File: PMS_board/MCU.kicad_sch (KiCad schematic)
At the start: 0 parts

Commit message: added buzzer? looked into stuff
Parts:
- added U13: STM32H563RITx, Package_QFP:LQFP-64_10x10mm_P0.5mm, symbol MCU_ST_STM32H5:STM32H563RITx
- added U6: (no value), MRDT_Shields:RoveNode_H5, symbol MRDT_Shields:RoveNode_H5
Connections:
- new net: U13.18 (VSS), U13.31 (VSS), U13.47 (VSS), U13.63 (VSS)
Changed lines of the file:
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@@
 	(generator_version "10.0")
 	(paper "A4")
-)

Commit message: TryingToFigureOutRoveNode
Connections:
- net PMSBus: now reaches U6.1 (VIN)
- net GND: now reaches U6.2 (GND)
- net out to Display: now reaches U6.23 (LED2)
- net out to Display: now also U6.24 (LED1), U6.42 (PB0), U6.43 (PB1)
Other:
- note added: "what is going on for microcontroller?"
- moved on the sheet: U13

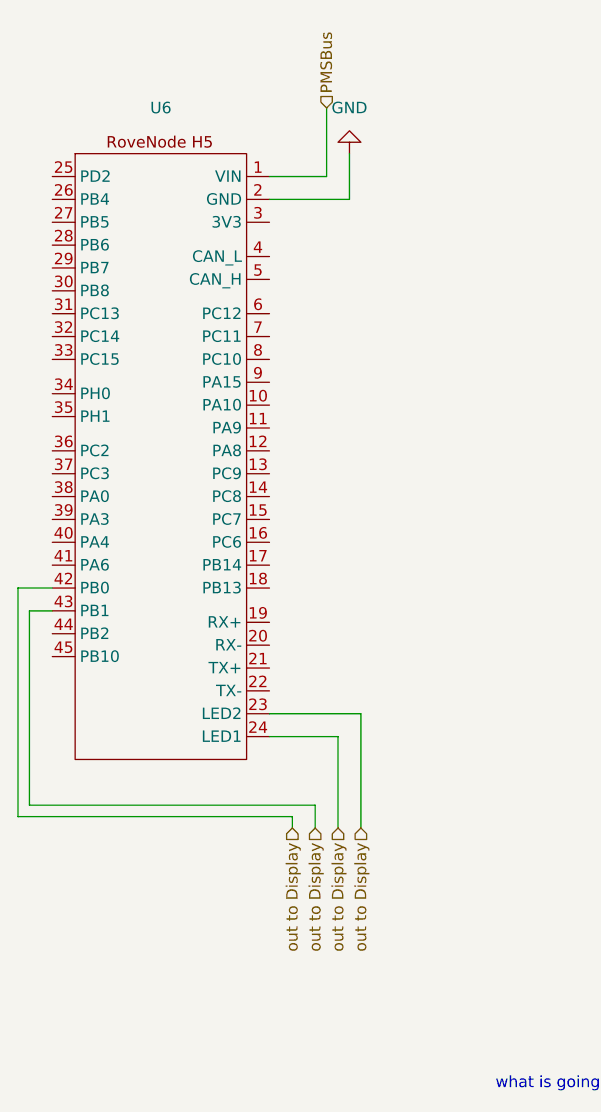
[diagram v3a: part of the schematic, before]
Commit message: addeddisplay
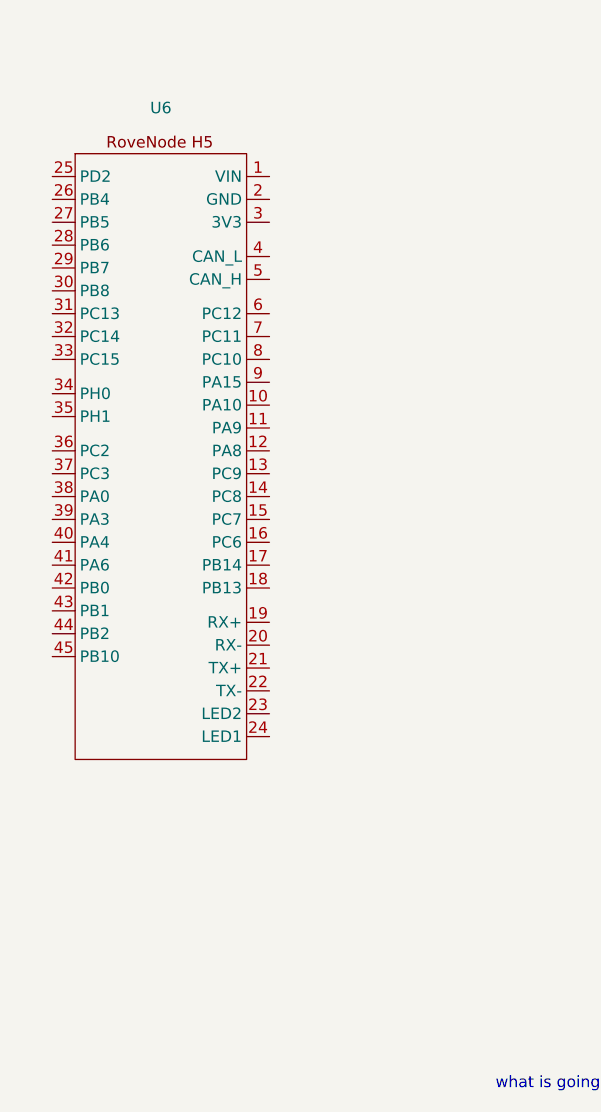
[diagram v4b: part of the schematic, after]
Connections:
- net GND: no longer names the net of U6.2 (GND)
- net PMSBus: no longer names the net of U6.1 (VIN)
- removed net out to Display: U6.23 (LED2), U6.24 (LED1), U6.42 (PB0), U6.43 (PB1)

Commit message: Fix Hotswap
I fixed hotswap, i think :)
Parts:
- removed U13: STM32H563RITx, Package_QFP:LQFP-64_10x10mm_P0.5mm, symbol MCU_ST_STM32H5:STM32H563RITx
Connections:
- net GND: now reaches U6.2 (GND)
- net +3V3: now reaches U6.3 (3V3)
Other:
- note removed: "what is going on for microcontroller?"

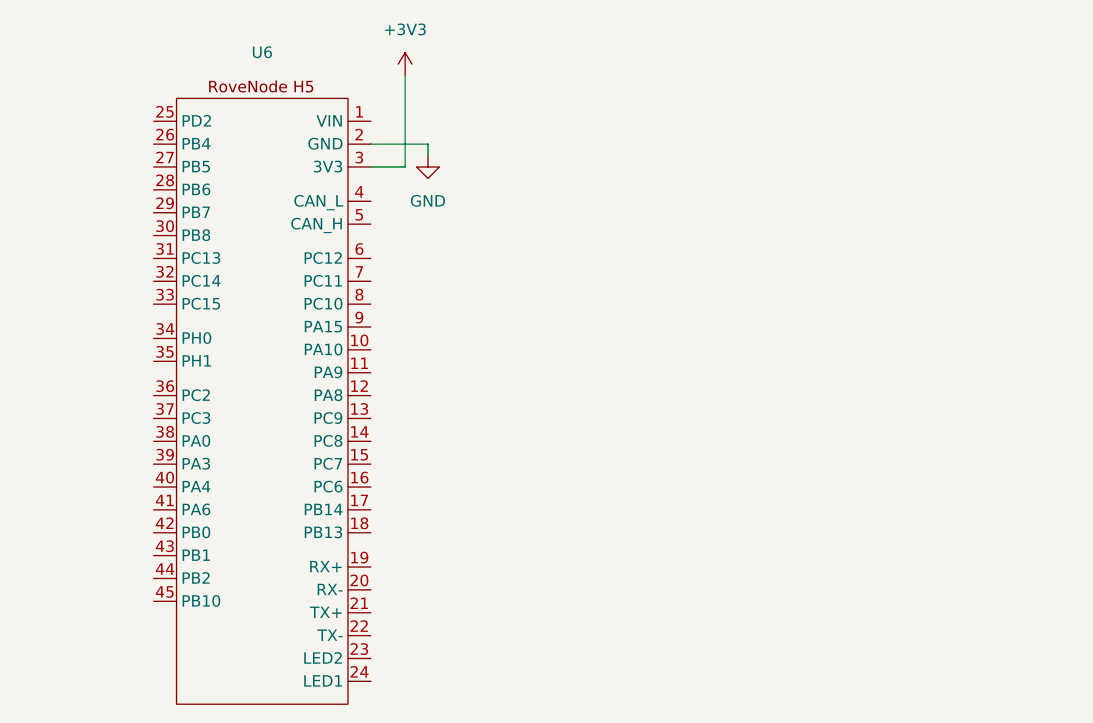
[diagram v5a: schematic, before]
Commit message: add microcontroller pinout
fixed hotswap, added pinouts to microcontroller, and made notes for power smoothing
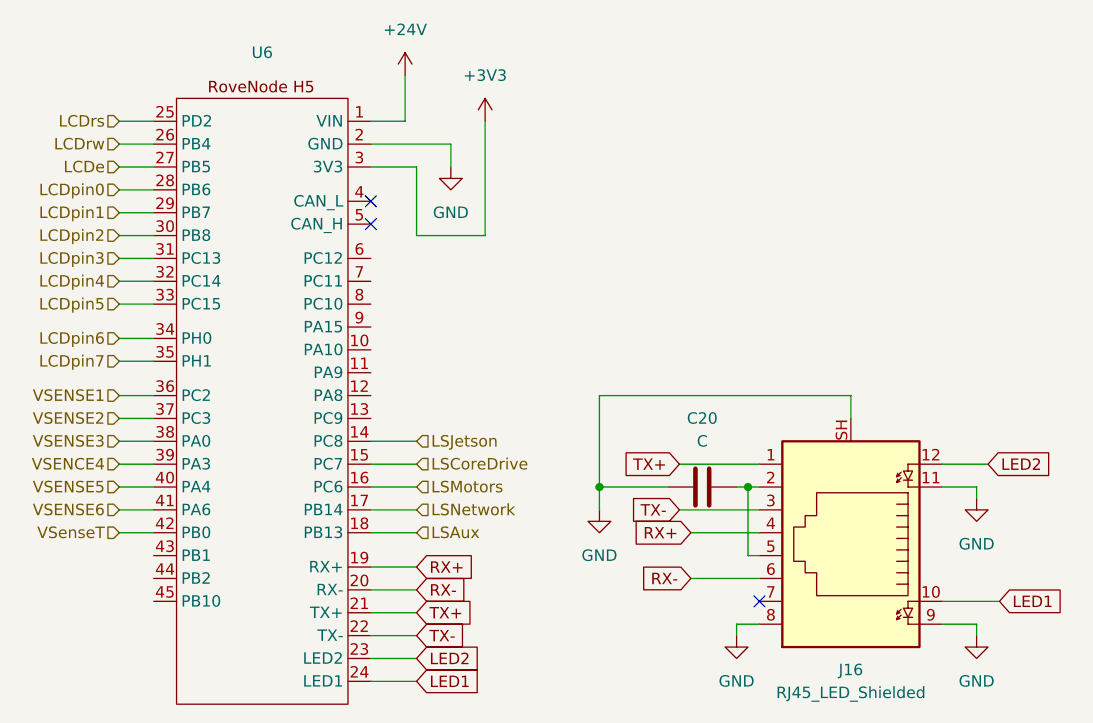
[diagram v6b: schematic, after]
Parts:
- added C20: C, symbol Device:C
- added J16: RJ45_LED_Shielded, symbol Connector:RJ45_LED_Shielded
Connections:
- net GND: now also C20.1, J16.11, J16.8, J16.9, J16.SH
- net +24V: now reaches U6.1 (VIN)
- net LSJetson: now reaches U6.14 (PC8)
- net LSCoreDrive: now reaches U6.15 (PC7)
- net LSMotors: now reaches U6.16 (PC6)
- net LSNetwork: now reaches U6.17 (PB14)
- net LSAux: now reaches U6.18 (PB13)
- net RX+: now reaches U6.19 (RX+)
- net RX+: now also J16.4
- net RX-: now reaches U6.20 (RX-)
- net RX-: now also J16.6
- net TX+: now reaches U6.21 (TX+)
- net TX+: now also J16.1
- net TX-: now reaches U6.22 (TX-)
- net TX-: now also J16.3
- net LED2: now reaches U6.23 (LED2)
- net LED2: now also J16.12
- net LED1: now reaches U6.24 (LED1)
- net LED1: now also J16.10
- net LCDrs: now reaches U6.25 (PD2)
- net LCDrw: now reaches U6.26 (PB4)
- net LCDe: now reaches U6.27 (PB5)
- net LCDpin0: now reaches U6.28 (PB6)
- net LCDpin1: now reaches U6.29 (PB7)
- net LCDpin2: now reaches U6.30 (PB8)
- net LCDpin3: now reaches U6.31 (PC13)
- net LCDpin4: now reaches U6.32 (PC14)
- net LCDpin5: now reaches U6.33 (PC15)
- net LCDpin6: now reaches U6.34 (PH0)
- net LCDpin7: now reaches U6.35 (PH1)
- net VSENSE1: now reaches U6.36 (PC2)
- net VSENSE2: now reaches U6.37 (PC3)
- net VSENSE3: now reaches U6.38 (PA0)
- net VSENCE4: now reaches U6.39 (PA3)
- net VSENSE5: now reaches U6.40 (PA4)
- net VSENSE6: now reaches U6.41 (PA6)
- net VSenseT: now reaches U6.42 (PB0)
- new net: C20.2, J16.2, J16.5
- no-connect marks 0 -> 3

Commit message: add converter and friends
I added the converter symbols and updated the schematic. I chose the proper FETs and Diodes for ORing circuit.
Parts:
- C20: value C -> 0.1uF
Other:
- note added: "heirarchial labels still need to be put on exterior of sheet"
- moved on the sheet: C20, J16, U6

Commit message: Finish Schematic
There's definitely stuff I missed, but I'm tired so we can review later. For my members to keep track of things, these are the changes/last minute additions I ran out of time to teach:
- brake chopper circuitry & reverse voltage protection for aux & motor rails
- microcontroller pinnouts
- net connections between sheets
- voltage resistors & system voltage measurements
- cell sense connectors & switch
- ADC routing
Please Please PLEASE ask questions about these additions. I don't want you guys to feel like you don't own this schematic, and I'm sorry I had to take away some of these designs to finish early. I definitely left too much on your plate to get everything perfect, which is my bad. I will happily walk through each and every circuit and help explain each part so you can better know your project when we get to reviewing and debugging later down the line.
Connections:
- net Buzzer: now reaches U6.10 (PA10)
- net Fault_Brake: now reaches U6.11 (PA9)
- net SenAux: now reaches U6.12 (PA8)
- net SenMotors: now reaches U6.13 (PC9)
- net CurrSenseT: now reaches U6.43 (PB1)
- net MOSI: now reaches U6.44 (PB2)
- net MISO: now reaches U6.7 (PC11)
- net SPI_SCK: now reaches U6.8 (PC10)
- net CS: now reaches U6.9 (PA15)
- net VSENCE4 renamed VSENSE4
- no-connect marks 3 -> 5
